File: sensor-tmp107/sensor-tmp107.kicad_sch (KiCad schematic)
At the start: 11 parts, among them J1 DE9_Socket_MountingHoles, J2 DE9_Socket_MountingHoles, Q1 SS8050, Q2 SS8050, U1 TMP107BIDR

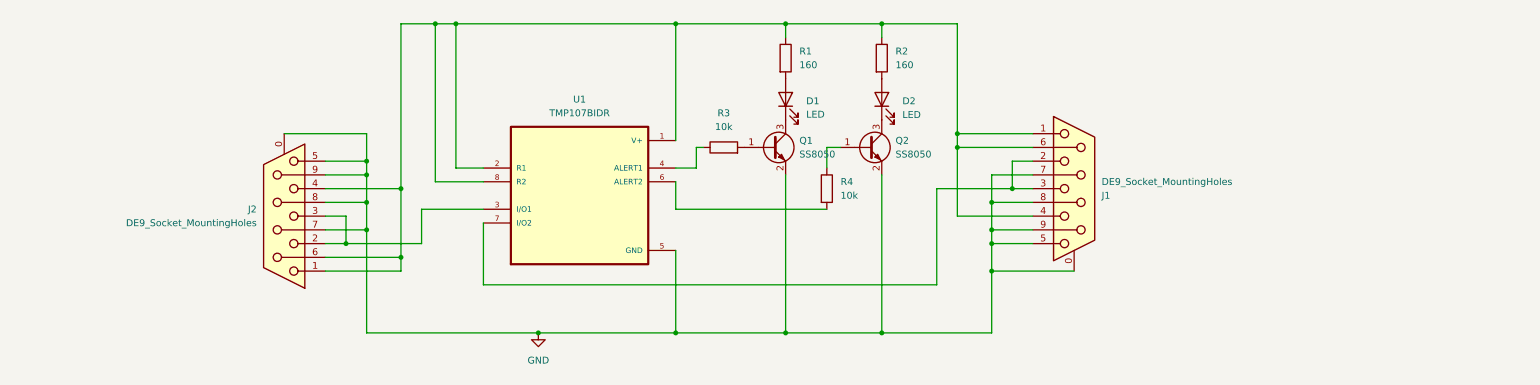
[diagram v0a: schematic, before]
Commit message: Added capcaitors, text improvements
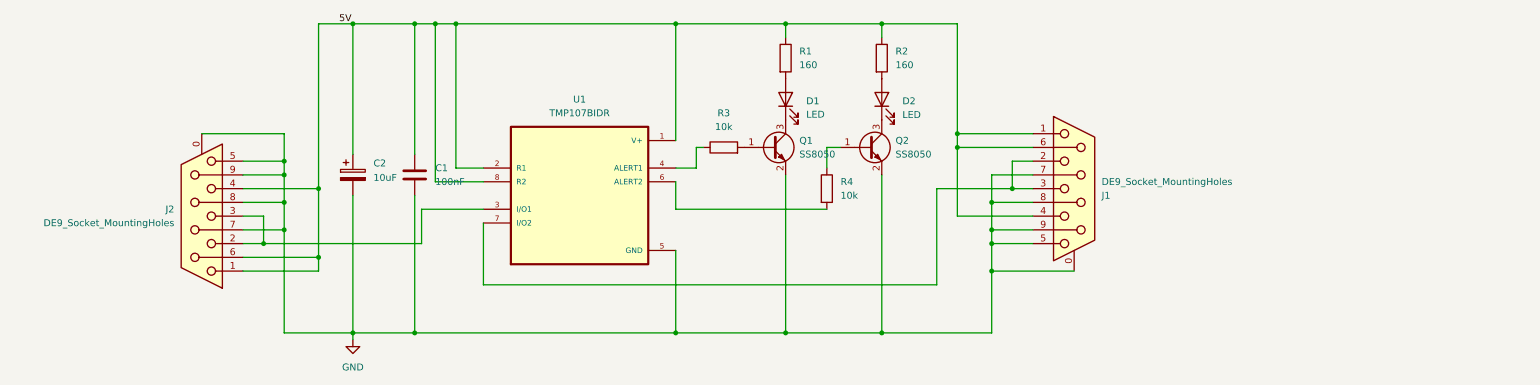
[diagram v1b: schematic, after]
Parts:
- added C1: 100nF, Capacitor_SMD:C_0805_2012Metric, symbol Device:C
- added C2: 10uF, Capacitor_SMD:CP_Elec_4x5.4, symbol Device:C_Polarized
- D1, D2: footprint LED_SMD:LED_0805_2012Metric_Pad1.15x1.40mm_HandSolder -> Diode_SMD:D_MiniMELF_Handsoldering
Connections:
- net GND: now also C1.2, C2.2
- net 5V: now reaches J1.1, J1.4, J1.6, J2.1, J2.4, J2.6, R1.1, R2.1, U1.1 (V+), U1.2 (R1), U1.8 (R2)
- net 5V: now also C1.1, C2.1
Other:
- moved on the sheet: J2

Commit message: Update sensor pcb
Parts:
- D1, D2: footprint Diode_SMD:D_MiniMELF_Handsoldering -> LED_SMD:LED_0805_2012Metric
- R1, R2, R3, R4: footprint Resistor_SMD:R_0805_2012Metric_Pad1.20x1.40mm_HandSolder -> Resistor_SMD:R_0805_2012Metric
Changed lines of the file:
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@@
 			)
 		)
-		(property "Footprint" "Resistor_SMD:R_0805_2012Metric_Pad1.20x1.40mm_HandSolder"
+		(property "Footprint" "Resistor_SMD:R_0805_2012Metric"
 			(at 165.862 69.85 90)
 			(effects
@@
 			)
 		)
-		(property "Footprint" "Resistor_SMD:R_0805_2012Metric_Pad1.20x1.40mm_HandSolder"
+		(property "Footprint" "Resistor_SMD:R_0805_2012Metric"
 			(at 155.702 93.98 90)
 			(effects
@@
 			)
 		)
-		(property "Footprint" "Diode_SMD:D_MiniMELF_Handsoldering"
+		(property "Footprint" "LED_SMD:LED_0805_2012Metric"
 			(at 167.64 77.47 0)
 			(effects
@@
 			)
 		)
-		(property "Footprint" "Resistor_SMD:R_0805_2012Metric_Pad1.20x1.40mm_HandSolder"
+		(property "Footprint" "Resistor_SMD:R_0805_2012Metric"
 			(at 148.082 69.85 90)
 			(effects
@@
 			)
 		)
-		(property "Footprint" "Diode_SMD:D_MiniMELF_Handsoldering"
+		(property "Footprint" "LED_SMD:LED_0805_2012Metric"
 			(at 149.86 77.47 0)
 			(effects
@@
 			)
 		)
-		(property "Footprint" "Resistor_SMD:R_0805_2012Metric_Pad1.20x1.40mm_HandSolder"
+		(property "Footprint" "Resistor_SMD:R_0805_2012Metric"
 			(at 138.43 88.138 90)
 			(effects

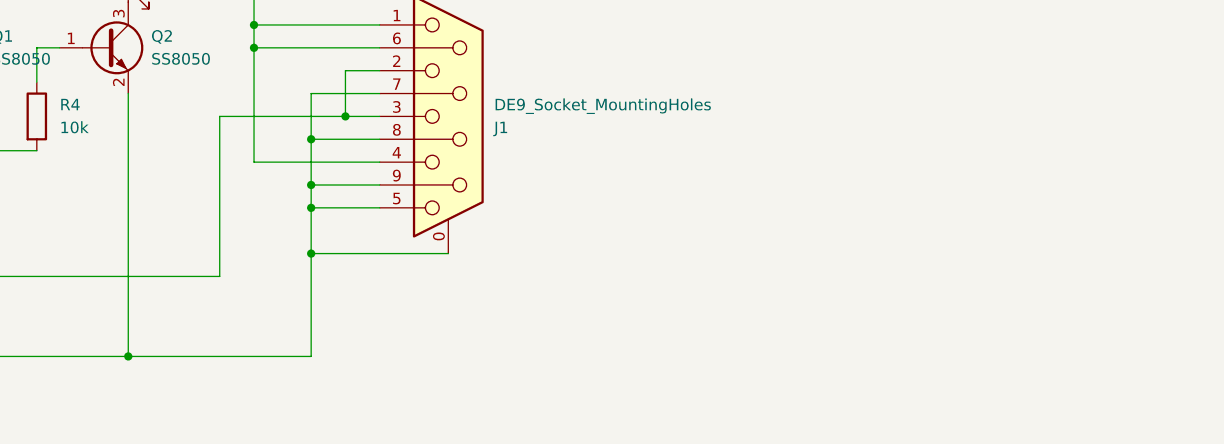
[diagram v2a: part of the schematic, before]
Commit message: Fix rs232 port footprint
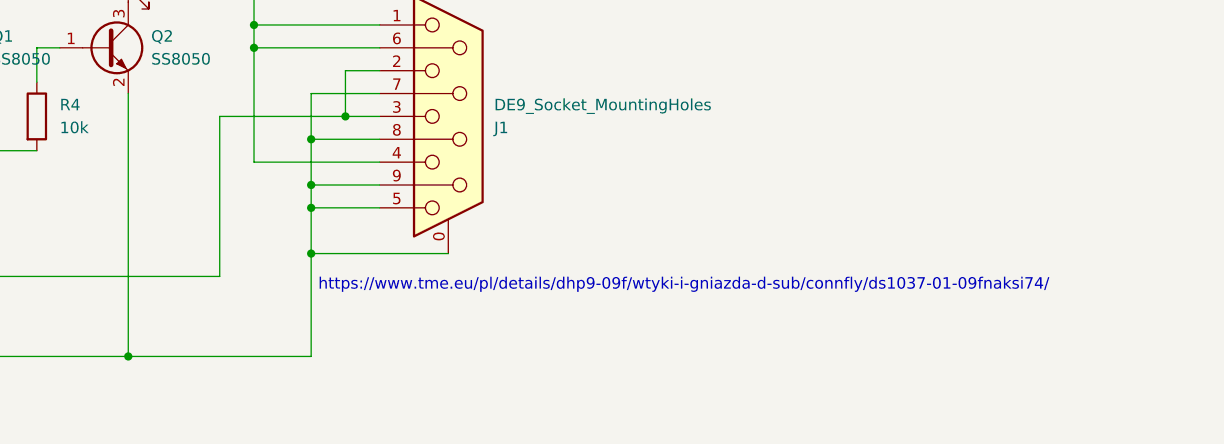
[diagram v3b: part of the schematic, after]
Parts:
- J1: footprint Connector_Dsub:DSUB-9_Socket_Horizontal_P2.77x2.84mm_EdgePinOffset4.94mm_Housed_MountingHolesOffset4.94mm -> Connector_Dsub:DSUB-9_Socket_Horizontal_P2.77x2.84mm_EdgePinOffset9.90mm_Housed_MountingHolesOffset11.32mm; tme (none) -> https://www.tme.eu/pl/details/dhp9-09f/wtyki-i-gniazda-d-su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
- J2: footprint Connector_Dsub:DSUB-9_Socket_Horizontal_P2.77x2.84mm_EdgePinOffset4.94mm_Housed_MountingHolesOffset4.94mm -> Connector_Dsub:DSUB-9_Socket_Horizontal_P2.77x2.84mm_EdgePinOffset9.90mm_Housed_MountingHolesOffset11.32mm
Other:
- note added: "https://www.tme.eu/pl/details/dhp9-09f/wtyki-i-gniazda-d-sub/connfly/ds1037-01-09fnaksi74/"
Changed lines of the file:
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@@
 	(generator_version "9.0")
 	(paper "A4")
+	(text "https://www.tme.eu/pl/details/dhp9-09f/wtyki-i-gniazda-d-sub/connfly/ds1037-01-09fnaksi74/\n"
+		(exclude_from_sim no)
+		(at 229.362 112.776 0)
+		(effects
+			(font
+				(size 1.27 1.27)
+			)
+		)
+	)
 	(junction
 		(at 149.86 63.5)
@@
 			)
 		)
-		(property "Footprint" "Connector_Dsub:DSUB-9_Socket_Horizontal_P2.77x2.84mm_EdgePinOffset4.94mm_Housed_MountingHolesOffset4.94mm"
+		(property "Footprint" "Connector_Dsub:DSUB-9_Socket_Horizontal_P2.77x2.84mm_EdgePinOffset9.90mm_Housed_MountingHolesOffset11.32mm"
 			(at 41.91 99.06 0)
 			(effects
@@
 			)
 		)
-		(property "Footprint" "Connector_Dsub:DSUB-9_Socket_Horizontal_P2.77x2.84mm_EdgePinOffset4.94mm_Housed_MountingHolesOffset4.94mm"
+		(property "Footprint" "Connector_Dsub:DSUB-9_Socket_Horizontal_P2.77x2.84mm_EdgePinOffset9.90mm_Housed_MountingHolesOffset11.32mm"
 			(at 203.2 93.98 0)
 			(effects
@@
 			(at 203.2 93.98 0)
 			(effects
+				(font
+					(size 1.27 1.27)
+				)
+				(hide yes)
+			)
+		)
+		(property "tme" "https://www.tme.eu/pl/details/dhp9-09f/wtyki-i-gniazda-d-sub/connfly/ds1037-01-09fnaksi74/"
+			(at 203.2 93.98 0)
+			(effects

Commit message: Update missing component values
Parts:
- D1: value LED -> LED żółtozielony
- D2: value LED -> LED czerwony
- R1, R2: value 160 -> 200
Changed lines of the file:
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@@
 			)
 		)
-		(property "Value" "160"
+		(property "Value" "200"
 			(at 170.18 71.1199 0)
 			(effects
@@
 			)
 		)
-		(property "Value" "LED"
+		(property "Value" "LED czerwony"
 			(at 171.45 80.3274 90)
 			(effects
@@
 			)
 		)
-		(property "Value" "160"
+		(property "Value" "200"
 			(at 152.4 71.1199 0)
 			(effects
@@
 			)
 		)
-		(property "Value" "LED"
+		(property "Value" "LED żółtozielony"
 			(at 153.67 80.264 90)
 			(effects
